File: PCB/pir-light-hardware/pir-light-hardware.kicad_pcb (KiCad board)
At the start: 2 copper layers, 8 parts, among them Q1 NMOS, U1 M74VHC1GT08DFT2G, U2 LMV331IDCKR

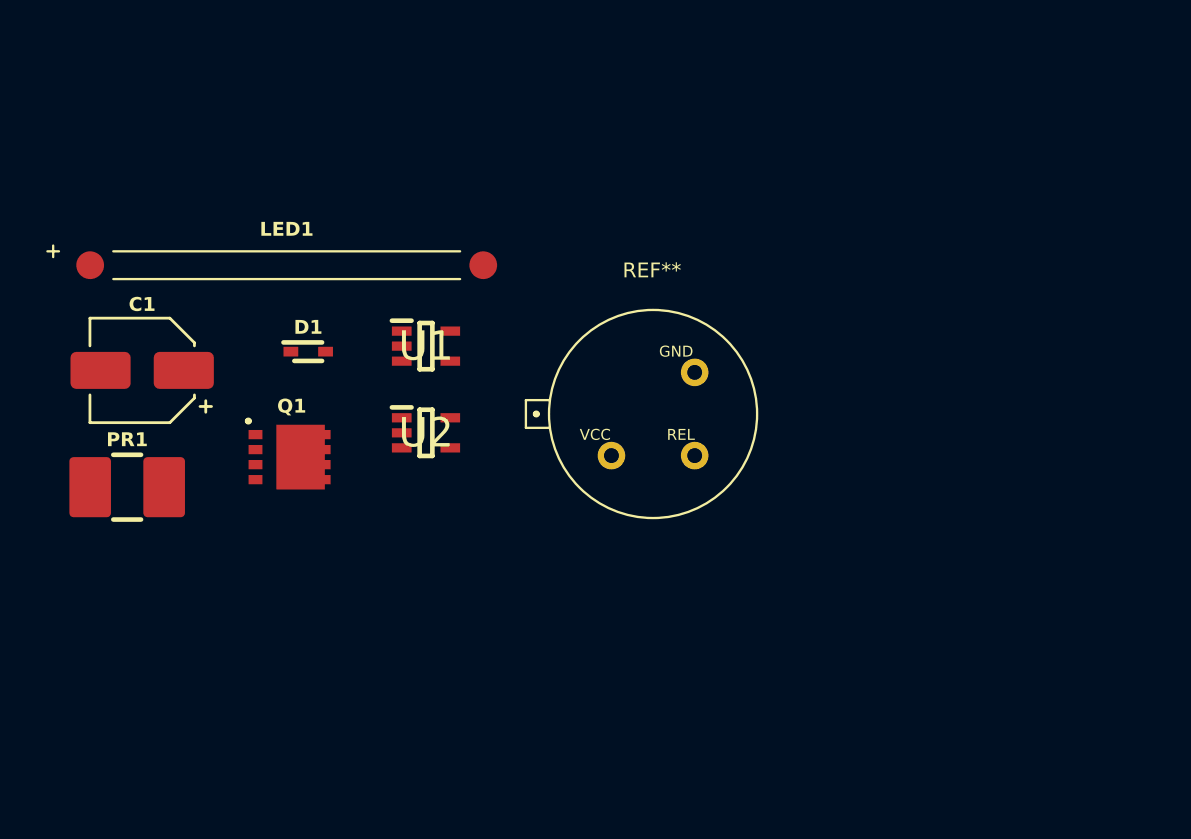
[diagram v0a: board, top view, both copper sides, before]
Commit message: chore: add power and signal sockets
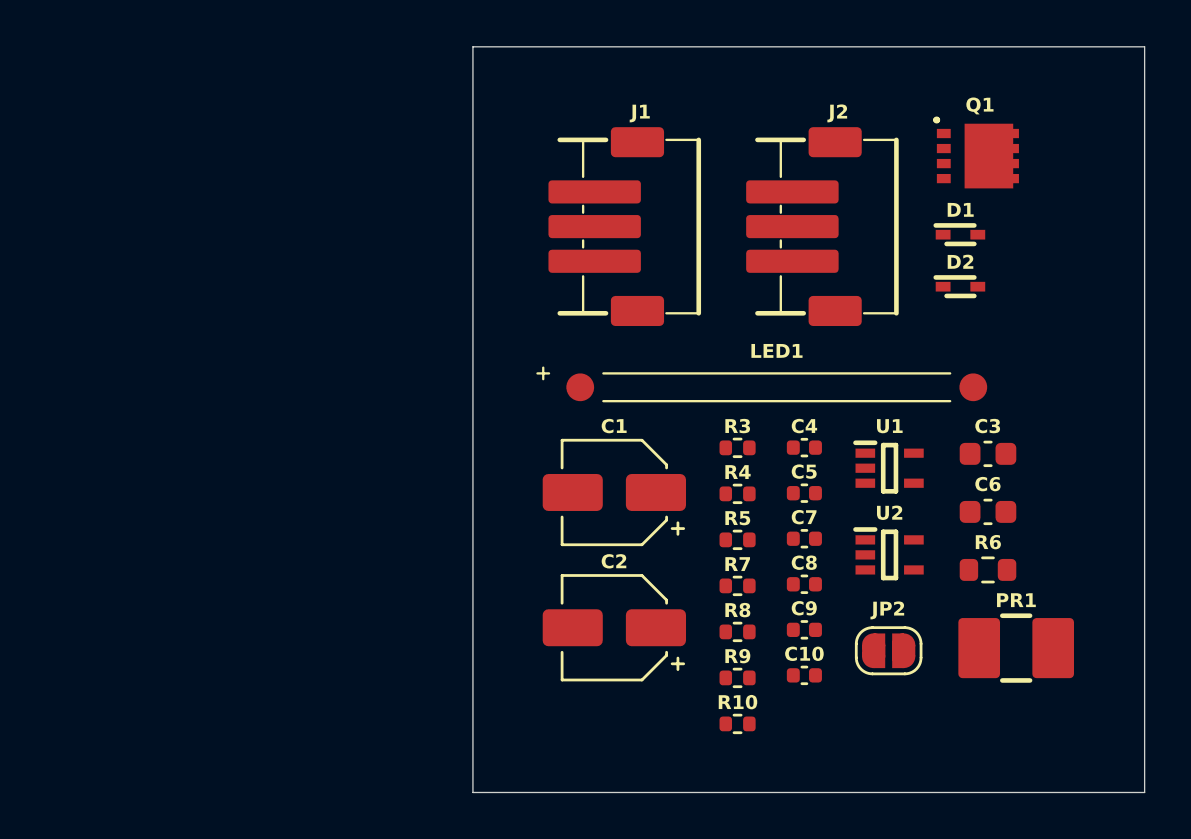
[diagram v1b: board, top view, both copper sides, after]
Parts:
- removed REF**: AS312-NEW, AS312:AS312-NEW
- added C10: 100nF, REST:C_0402_1005Metric, F.Cu at (190.8, 104.4)
- added C2: 47uF, REST:CP_Elec_4x5.4, F.Cu at (182.6, 102.4)
- added C3: 10uF, REST:C_0603_1608Metric, F.Cu at (198.7, 94.8)
- added C4: 10nF, REST:C_0402_1005Metric, F.Cu at (190.8, 94.6)
- added C5: 100nF, REST:C_0402_1005Metric, F.Cu at (190.8, 96.5)
- added C6: 10uF, REST:C_0603_1608Metric, F.Cu at (198.7, 97.3)
- added C7: 100nF, REST:C_0402_1005Metric, F.Cu at (190.8, 98.5)
- added C8: 100nF, REST:C_0402_1005Metric, F.Cu at (190.8, 100.5)
- added C9: 100nF, REST:C_0402_1005Metric, F.Cu at (190.8, 102.4)
- added D2: 1N5819HWQ-7-F, 1N5819HWQ-7-F:1N5819HWQ-7-F, F.Cu at (197.5, 87.6)
- added J1: ZH1.5-3, ZH-CONNECTOR:ZH1.5-3, F.Cu at (183.7, 85.0)
- added J2: ZH1.5-3, ZH-CONNECTOR:ZH1.5-3, F.Cu at (192.3, 85.0)
- added JP2: Jumper_Open, REST:SolderJumper-2_P1.3mm_Open_RoundedPad1.0x1.5mm, F.Cu at (194.4, 103.3)
- added R10: R, REST:R_0402_1005Metric, F.Cu at (187.9, 106.5)
- added R3: 1MR, REST:R_0402_1005Metric, F.Cu at (187.9, 94.6)
- added R4: 620kR, REST:R_0402_1005Metric, F.Cu at (187.9, 96.6)
- added R5: 1MR, REST:R_0402_1005Metric, F.Cu at (187.9, 98.6)
- added R6: 0R, REST:R_0603_1608Metric, F.Cu at (198.7, 99.9)
- added R7: 100kR, REST:R_0402_1005Metric, F.Cu at (187.9, 100.5)
- added R8: 10kR, REST:R_0402_1005Metric, F.Cu at (187.9, 102.5)
- added R9: R, REST:R_0402_1005Metric, F.Cu at (187.9, 104.5)
- C1: value C -> 33uF
- Q1: value NMOS -> AON7240
- moved PR1 39.1 mm to (199.9, 103.2)
- moved Q1 32.5 mm to (198.4, 82.0)
- moved D1 28.7 mm to (197.5, 85.4)
- moved LED1 21.8 mm to (189.6, 92.0)
- moved C1 21.1 mm to (182.6, 96.5)
- moved U1 20.7 mm to (194.5, 95.5)
- moved U2 20.7 mm to (194.5, 99.2)
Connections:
- C1 pad 1: unconnected-(C1-Pad1) -> Net-(D1-K)
- C1 pad 2: unconnected-(C1-Pad2) -> GND
- D1 pad 1: unconnected-(D1-K-Pad1) -> Net-(D1-K)
- D1 pad 2: unconnected-(D1-A-Pad2) -> Net-(D1-A)
- LED1 pad 1: unconnected-(LED1-Pad1) -> Net-(LED1-Pad1)
- LED1 pad 2: unconnected-(LED1-Pad2) -> Net-(Q1-D)
- PR1 pad 1: unconnected-(PR1-Pad1) -> /LLS
- PR1 pad 2: unconnected-(PR1-Pad2) -> GND
- Q1 pad 1: unconnected-(Q1-S-Pad1) -> GND
- Q1 pad 2: unconnected-(Q1-G-Pad2) -> Net-(JP2-A)
- Q1 pad 3: unconnected-(Q1-D-Pad3) -> Net-(Q1-D)
- U1 pad 1: unconnected-(U1A-B-Pad1) -> Net-(U1A-B)
- U1 pad 2: unconnected-(U1A-A-Pad2) -> /PIR
- U1 pad 3: unconnected-(U1B-GND-Pad3) -> GND
- U1 pad 4: unconnected-(U1A-Y-Pad4) -> Net-(D1-A)
- U1 pad 5: unconnected-(U1B-VCC-Pad5) -> 3V3
- U2 pad 1: unconnected-(U2A-+-Pad1) -> /LLS
- U2 pad 3: unconnected-(U2A---Pad3) -> /REF
- U2 pad 4: unconnected-(U2-Pad4) -> GND
- U2 pad 5: unconnected-(U2B-VCC-Pad5) -> 3V3
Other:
- board outline added: 29.1 x 32.2 mm
